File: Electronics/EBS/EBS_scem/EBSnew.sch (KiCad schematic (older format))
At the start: 24 parts

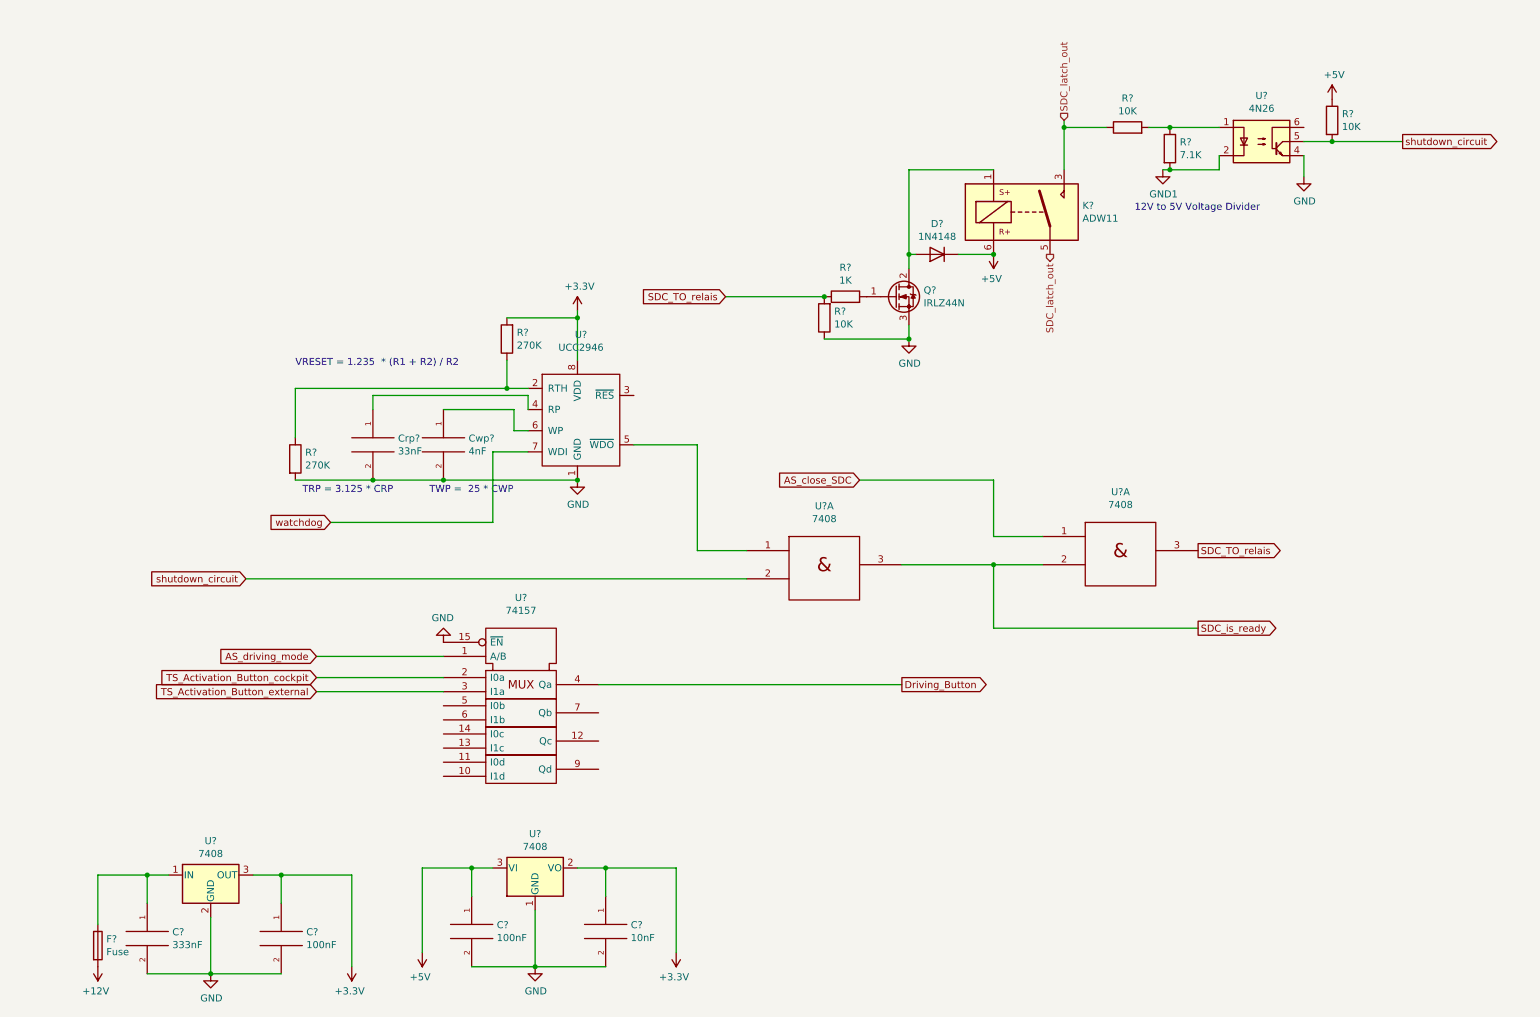
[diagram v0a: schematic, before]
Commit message: EBS,TSAL, and activation
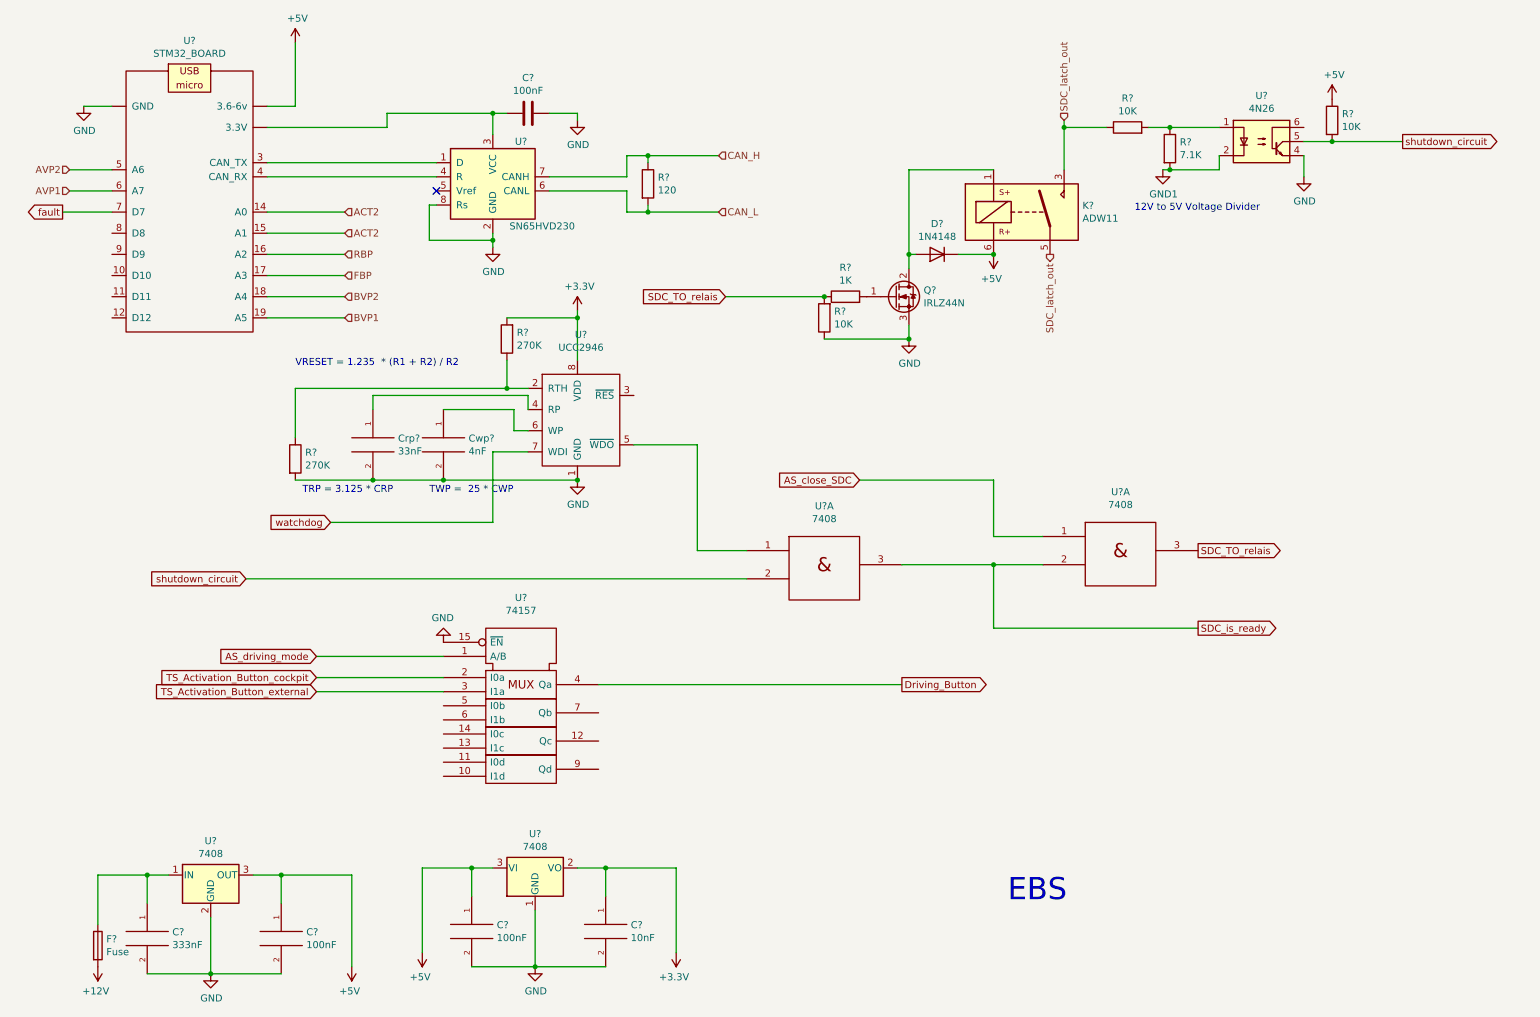
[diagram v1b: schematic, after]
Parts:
- added C?: 100nF, symbol Device:C
- added R?: 120, symbol Device:R
- added U?: SN65HVD230, Package_SO:SOIC-8_3.9x4.9mm_P1.27mm, symbol Interface_CAN_LIN:SN65HVD230
- added U?: STM32_BOARD, symbol EBS_library:STM32_BOARD
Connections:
- net +3V3: no longer C?.1, U?.3 (OUT)
- net +5V: now also C?.1, U?.3 (OUT), U?.~ (GND)
- net GND: now also C?.1, U?.2 (GND), U?.8 (Rs), U?.~ (GND)
- new net: U?.1 (D), U?.3 (CAN_TX)
- new net: C?.2, U?.3 (VCC), U?.~ (GND)
- new net: U?.4 (CAN_RX), U?.4 (R)
- new net ACT2: U?.14 (A0), U?.15 (A1)
- new net AVP1: U?.6 (A7)
- new net AVP2: U?.5 (A6)
- new net BVP1: U?.19 (A5)
- new net BVP2: U?.18 (A4)
- new net CAN_H: R?.1, U?.7 (CANH)
- new net CAN_L: R?.2, U?.6 (CANL)
- new net FBP: U?.17 (A3)
- new net RBP: U?.16 (A2)
- new net fault: U?.7 (D7)
- no-connect marks 0 -> 1
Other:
- note added: "EBS"
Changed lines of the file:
@@
 Wire Wire Line
 	2500 6950 2500 6750
-$Comp
-L power:+3.3V #PWR?
-U 1 1 600A3F9A
-P 3000 7400
-F 0 "#PWR?" H 3000 7250 50  0001 C CNN
-F 1 "+3.3V" H 3015 7573 50  0000 C CNN
-F 2 "" H 3000 7400 50  0001 C CNN
-F 3 "" H 3000 7400 50  0001 C CNN
-	1    3000 7400
-	-1   0    0    1
-$EndComp
 Wire Wire Line
 	2300 6750 2500 6750
@@
 Text GLabel 6900 5400 2    50   Output ~ 0
 Driving_Button
+Text Notes 7650 6950 0    157  ~ 0
+EBS
+Wire Wire Line
+	3250 1350 3250 1450
+Text HLabel 2950 2050 2    50   Input ~ 0
+ACT2
+Text HLabel 2950 2200 2    50   Input ~ 0
+ACT2
+Text HLabel 2950 2350 2    50   Input ~ 0
+RBP
+Text HLabel 2950 2500 2    50   Input ~ 0
+FBP
+Text HLabel 2950 2650 2    50   Input ~ 0
+BVP2
+Text HLabel 2950 2800 2    50   Input ~ 0
+BVP1
+Text HLabel 1000 1750 0    50   Input ~ 0
+AVP2
+Text HLabel 1000 1900 0    50   Input ~ 0
+AVP1
+$Comp
+L power:GND #PWR?
+U 1 1 60084923
+P 1100 1300
+F 0 "#PWR?" H 1100 1050 50  0001 C CNN
+F 1 "GND" H 1105 1127 50  0000 C CNN
+F 2 "" H 1100 1300 50  0001 C CNN
+F 3 "" H 1100 1300 50  0001 C CNN
+	1    1100 1300
+	1    0    0    -1
+$EndComp
+Wire Wire Line
+	1300 1300 1100 1300
+$Comp
+L EBS_library:STM32_BOARD U?
+U 1 1 60094702
+P 1850 1600
+F 0 "U?" H 1850 2365 50  0000 C CNN
+F 1 "STM32_BOARD" H 1850 2274 50  0000 C CNN
+F 2 "" H 1850 1450 50  0001 C CNN
+F 3 "" H 1850 1450 50  0001 C CNN
+	1    1850 1600
+	1    0    0    -1
+$EndComp
+Wire Wire Line
+	1000 1750 1300 1750
+Text GLabel 950  2050 0    50   Output ~ 0
+fault
+Wire Wire Line
+	1300 2050 950  2050
+Wire Wire Line
+	2600 1300 2400 1300
+Wire Wire Line
+	3250 1450 2400 1450
+Wire Wire Line
+	2400 2050 2950 2050
+Wire Wire Line
+	2950 2200 2400 2200
+Wire Wire Line
+	2400 2350 2950 2350
+Wire Wire Line
+	2950 2500 2400 2500
+Wire Wire Line
+	2400 2650 2950 2650
+Wire Wire Line
+	2950 2800 2400 2800
+$Comp
+L power:+5V #PWR?
+U 1 1 600812A9
+P 2600 850
+F 0 "#PWR?" H 2600 700 50  0001 C CNN
+F 1 "+5V" H 2615 1023 50  0000 C CNN
+F 2 "" H 2600 850 50  0001 C CNN
+F 3 "" H 2600 850 50  0001 C CNN
+	1    2600 850
+	1    0    0    -1
+$EndComp
+Wire Wire Line
+	2600 850  2600 1300
+$Comp
+L Interface_CAN_LIN:SN65HVD230 U?
+U 1 1 6008125E
+P 4000 1800
+F 0 "U?" H 4200 2050 50  0000 C CNN
+F 1 "SN65HVD230" H 4350 1450 50  0000 C CNN
+F 2 "Package_SO:SOIC-8_3.9x4.9mm_P1.27mm" H 4000 1300 50  0001 C CNN
+F 3 "http://www.ti.com/lit/ds/symlink/sn65hvd230.pdf" H 3900 2200 50  0001 C CNN
+	1    4000 1800
+	1    0    0    -1
+$EndComp
+Wire Wire Line
+	4000 2250 3550 2250
+Wire Wire Line
+	3550 2250 3550 2000
+Wire Wire Line
+	3550 2000 3600 2000
+NoConn ~ 3600 1900
+Wire Wire Line
+	3250 1350 4000 1350
+Wire Wire Line
+	3600 1700 2400 1700
+Wire Wire Line
+	2400 1800 3600 1800
+Wire Wire Line
+	4400 1800 4950 1800
+Wire Wire Line
+	4950 1900 4400 1900
+Wire Wire Line
+	4000 1350 4100 1350
+Connection ~ 4000 1350
+Wire Wire Line
+	4000 1500 4000 1350
+Wire Wire Line
+	5100 2050 4950 2050
+Connection ~ 5100 2050
+Wire Wire Line
+	5100 2000 5100 2050
+Wire Wire Line
+	5100 1650 5600 1650
+Connection ~ 5100 1650
+Wire Wire Line
+	5100 1700 5100 1650
+Wire Wire Line
+	4950 2050 4950 1900
+Wire Wire Line
+	5600 2050 5100 2050
+Wire Wire Line
+	4950 1650 5100 1650
+Wire Wire Line
+	4950 1800 4950 1650
+Text HLabel 5600 2050 2    50   Input ~ 0
+CAN_L
+Text HLabel 5600 1650 2    50   Input ~ 0
+CAN_H
+$Comp
+L Device:R R?
+U 1 1 60081283
+P 5100 1850
+F 0 "R?" H 5170 1896 50  0000 L CNN
+F 1 "120" H 5170 1805 50  0000 L CNN
+F 2 "" V 5030 1850 50  0001 C CNN
+F 3 "~" H 5100 1850 50  0001 C CNN
+	1    5100 1850
+	1    0    0    -1
+$EndComp
+Wire Wire Line
+	4600 1350 4400 1350
+Wire Wire Line
+	4600 1400 4600 1350
+$Comp
+L Device:C C?
+U 1 1 60081278
+P 4250 1350
+F 0 "C?" V 3998 1350 50  0000 C CNN
+F 1 "100nF" V 4089 1350 50  0000 C CNN
+F 2 "" H 4288 1200 50  0001 C CNN
+F 3 "~" H 4250 1350 50  0001 C CNN
+	1    4250 1350
+	0    1    1    0
+$EndComp
+$Comp
+L power:GND #PWR?
+U 1 1 60081272
+P 4600 1400
+F 0 "#PWR?" H 4600 1150 50  0001 C CNN
+F 1 "GND" H 4605 1227 50  0000 C CNN
+F 2 "" H 4600 1400 50  0001 C CNN
+F 3 "" H 4600 1400 50  0001 C CNN
+	1    4600 1400
+	1    0    0    -1
+$EndComp
+Wire Wire Line
+	4000 2250 4000 2200
+Connection ~ 4000 2250
+Wire Wire Line
+	4000 2300 4000 2250
+$Comp
+L power:GND #PWR?
+U 1 1 60081266
+P 4000 2300
+F 0 "#PWR?" H 4000 2050 50  0001 C CNN
+F 1 "GND" H 4005 2127 50  0000 C CNN
+F 2 "" H 4000 2300 50  0001 C CNN
+F 3 "" H 4000 2300 50  0001 C CNN
+	1    4000 2300
+	1    0    0    -1
+$EndComp
+Wire Wire Line
+	1300 1900 1000 1900
+$Comp
+L power:+5V #PWR?
+U 1 1 600A38BF
+P 3000 7400
+F 0 "#PWR?" H 3000 7250 50  0001 C CNN
+F 1 "+5V" H 3015 7573 50  0000 C CNN
+F 2 "" H 3000 7400 50  0001 C CNN
+F 3 "" H 3000 7400 50  0001 C CNN
+	1    3000 7400
+	-1   0    0    1
+$EndComp
 $EndSCHEMATC
